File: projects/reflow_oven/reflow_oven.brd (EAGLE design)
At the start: 80 x 36 mm, 34 parts, among them IC1 MEGA8-AI, IC2 7805DT, IC3 FT232RL, IC4 74HC14D, J1 1X2-3.5MM, SW1 RST SW, SW2 D3 SW, SW3 D2 SW, X1 USB, X2 16MHz

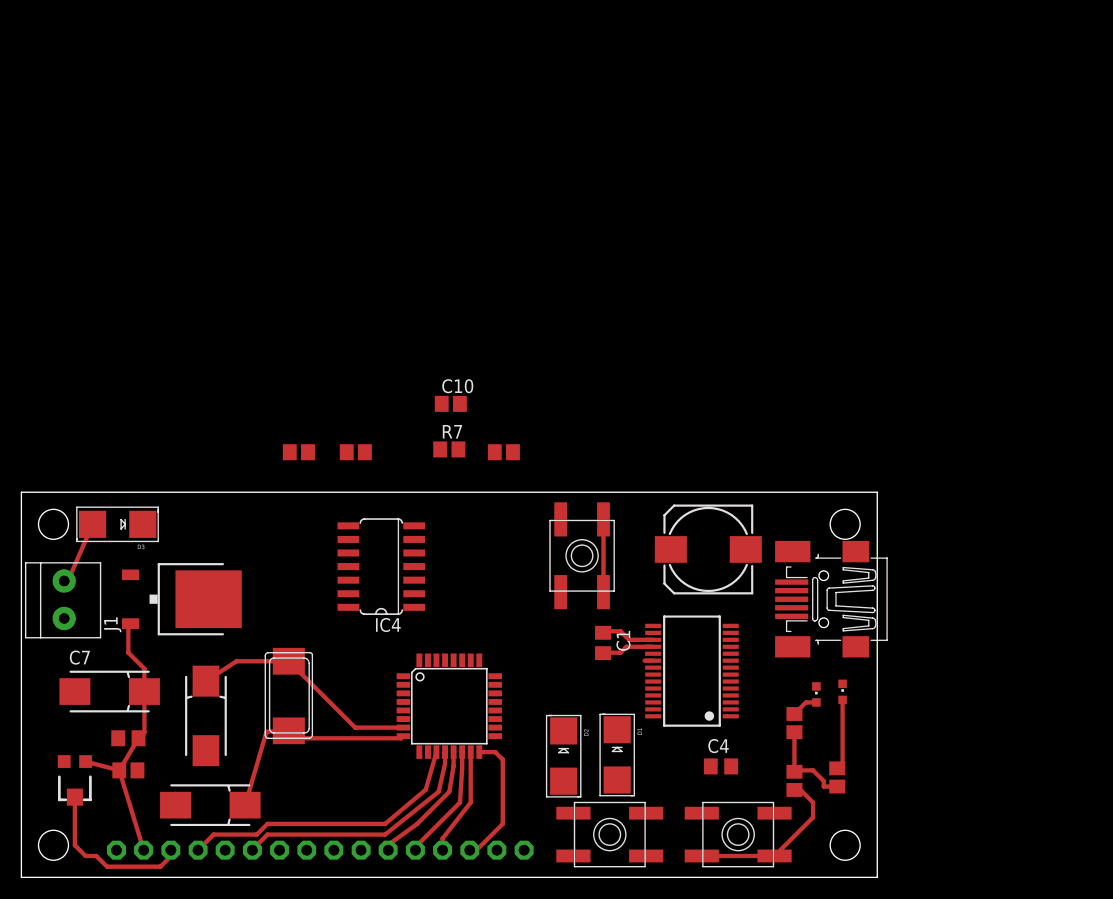
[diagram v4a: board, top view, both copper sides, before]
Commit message: changing parts again, now down to 0603 size
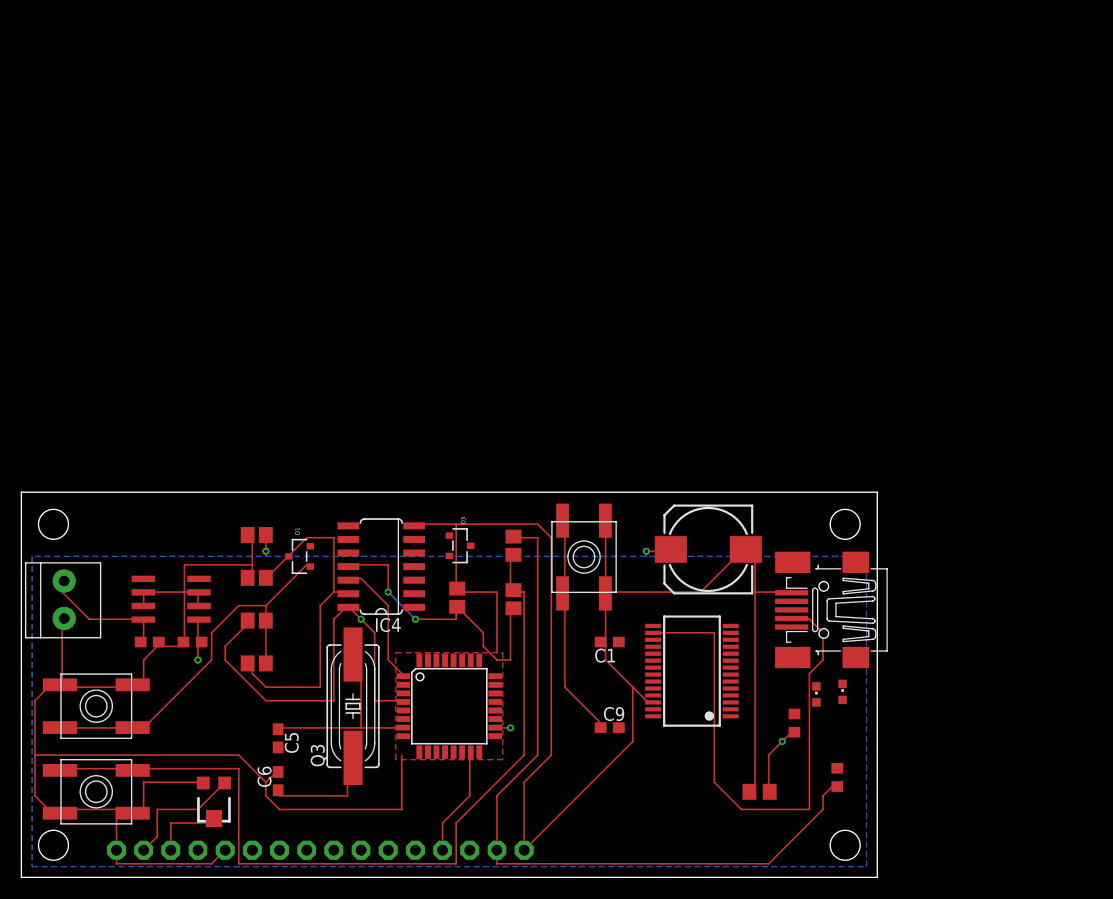
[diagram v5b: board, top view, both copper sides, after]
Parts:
- removed C4: 0.1uF, rcl:C0805
- removed D2: (no value), adafruit:SMADIODE
- removed X2: 16MHz, adafruit:NX8045
- added C8: 0.33uF, rcl:C0603
- added C9: (no value), rcl:C0603
- added Q3: 16MHz, crystal:SM49
- C1: value 0.1uF -> (none); device rcl:C0805 -> rcl:C0603
- C5, C6: value 22pF -> (none); device rcl:085CS_1AR -> rcl:C0603
- C7: value (none) -> 0.01uF; device rcl:085CS_1AR -> rcl:C0603
- D1, D3: value (none) -> 1N4148; device adafruit:SMADIODE -> adafruit:SOT23-R
- IC2: value 7805DT -> 78L05SMD; device linear:TO252 -> linear:SO08
- R1, R2: device resistor:R0805 -> resistor:R0603
- moved SW2 61.2 mm to (7.00, 16.0)
- moved C2 59.2 mm to (69.0, 8.00)
- moved R5 52.4 mm to (22.0, 24.0), turned to 0 degrees
- moved SW3 48.2 mm to (7.00, 8.00), turned to 0 degrees
- moved D1 35.0 mm to (26.0, 30.0), turned to 90 degrees
- moved D3 32.1 mm to (41.0, 31.0), turned to 270 degrees
- moved C12 25.1 mm to (22.0, 32.0), turned to 180 degrees
- moved R8 21.8 mm to (22.0, 20.0)
- moved C10 18.1 mm to (40.7, 26.1), turned to 90 degrees
- moved R7 15.2 mm to (46.0, 26.0), turned to 270 degrees
- moved U$1 13.2 mm to (18.0, 7.00)
- moved C11 12.4 mm to (22.0, 28.0)
- moved C7 9.03 mm to (16.0, 22.0), turned to 180 degrees
- moved R6 8.79 mm to (46.0, 31.0), turned to 270 degrees
- moved C5 7.07 mm to (24.0, 13.0), turned to 270 degrees
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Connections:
- removed net VIN: D3.C, IC2.1
- net 5V: now also C7.1, IC2.1; no longer C7.+, IC2.2
- net DTR: now also C9.2; no longer C4.2
- net GND: now also C5.2, C6.2, C7.2, C8.2, IC2.2, IC2.6, IC2.7; no longer C5.-, C6.-, C7.-
- net N$12: now also D1.1; no longer D1.A
- net N$13: now also D1.3; no longer D1.C
- net N$14: now also D3.1; no longer D2.A
- net N$15: now also D3.3; no longer D2.C
- net PWRIN: now also C8.1, IC2.8; no longer D3.A
- net RESET: now also C9.1; no longer C4.1
- net XTAL1: now also C5.1, Q3.2; no longer C5.+, X2.P$2
- net XTAL2: now also C6.1, Q3.1; no longer C6.+, X2.P$1
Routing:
- net GND: track 4.93 -> 283.2 mm
- net 5V: track 35.7 -> 141.0 mm, vias 0 -> 6
- net N$14: track 0.00 -> 79.9 mm
- net D-DM: track 0.00 -> 50.1 mm
- net N$13: track 0.00 -> 32.6 mm
- net N$15: track 0.00 -> 28.7 mm, vias 0 -> 2
- net 7: track 27.1 -> 0.00 mm
- net 8: track 23.3 -> 0.00 mm
- net N$12: track 15.5 -> 36.8 mm
- net RESET: track 8.05 -> 21.6 mm
- net 12: track 12.6 -> 0.00 mm
- net 3: track 0.00 -> 12.2 mm
- net 9: track 12.1 -> 0.00 mm
- net 10: track 10.9 -> 0.00 mm
- net XTAL2: track 20.3 -> 10.6 mm
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- added copper zone on layer 16, net 5V
- added copper zone on layer 1, net GND
